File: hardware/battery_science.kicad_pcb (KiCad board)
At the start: 2 copper layers, 61 x 44.5 mm, 49 parts, among them P201 CONN_01X06, P301 CONN_01X08, P401 CONN_01X05, P402 CONN_01X05, Q301 BSS84, SW201 SPST, SW202 SPST, U201 LPC11C14, U301 BQ76925, U401 ADS1148IPWR

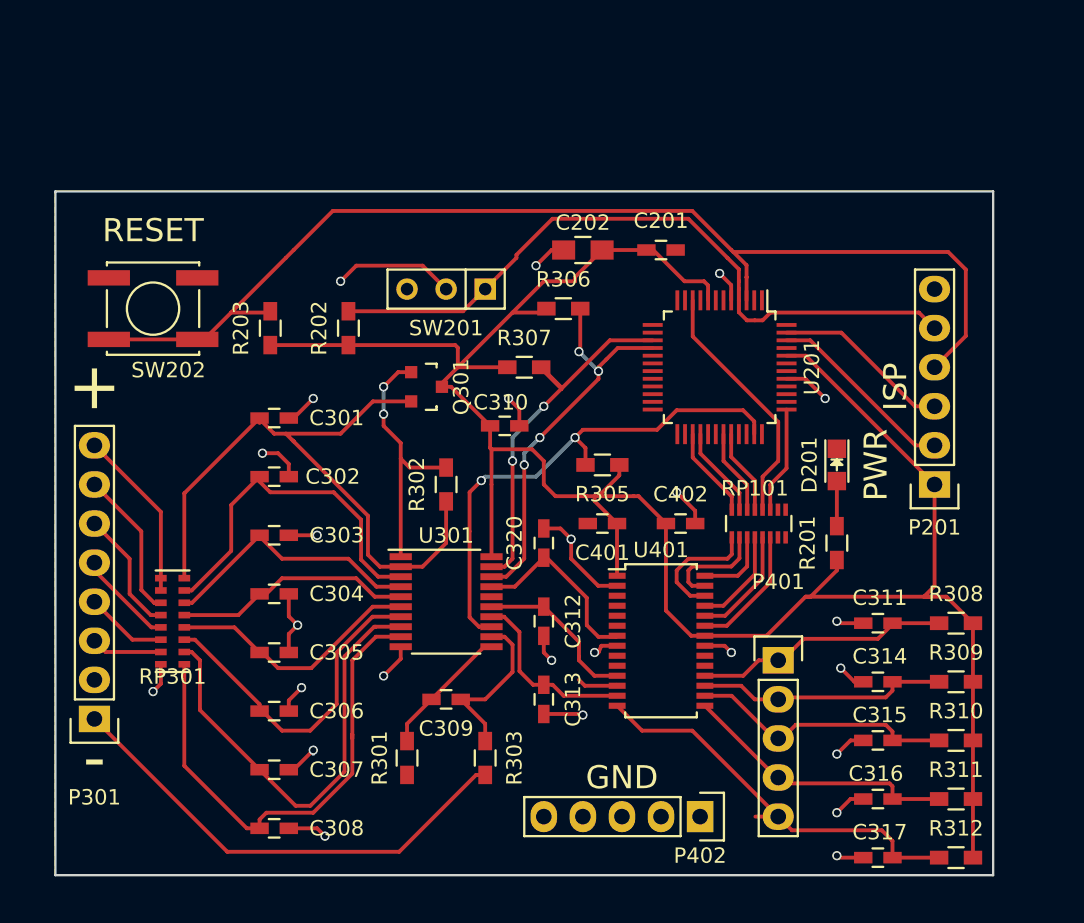
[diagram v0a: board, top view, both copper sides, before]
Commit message: Updated pcb layout
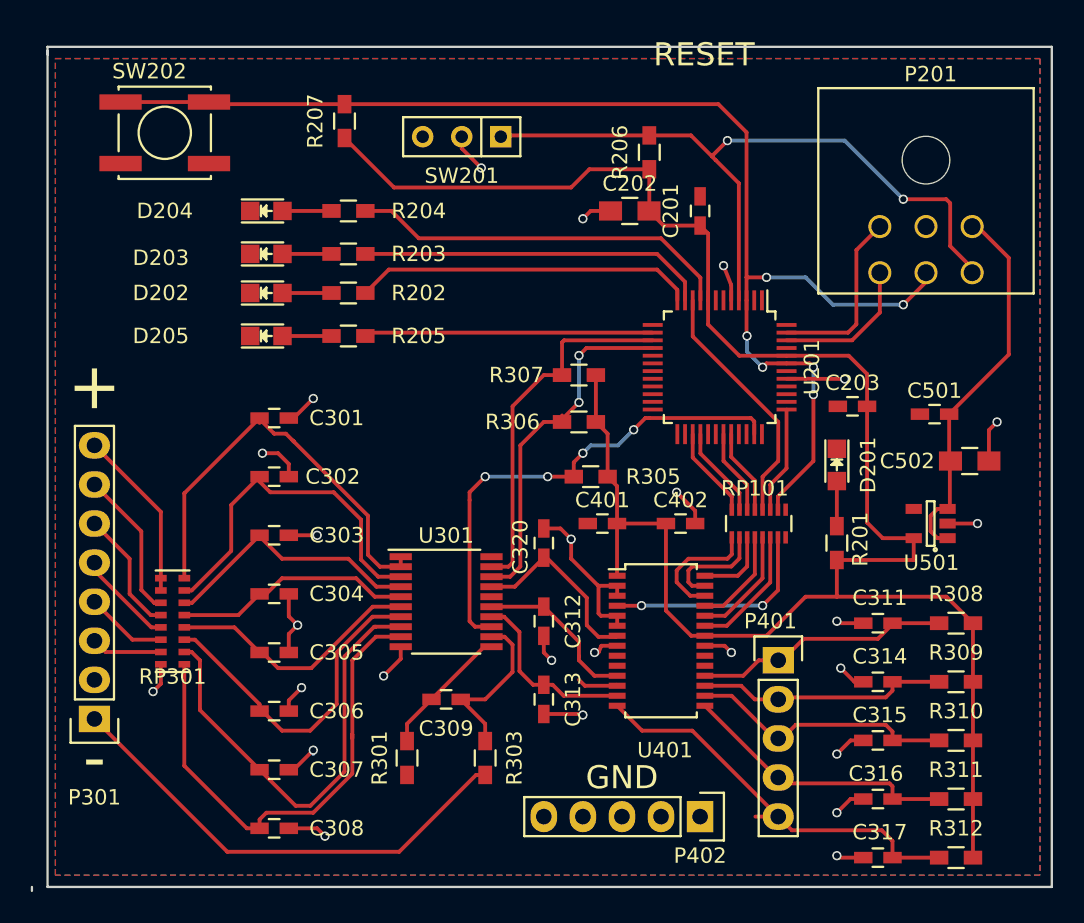
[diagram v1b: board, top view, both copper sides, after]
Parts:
- removed C310: 4.7μF, Capacitors_SMD:C_0603_HandSoldering
- removed Q301: BSS84, TO_SOT_Packages_SMD:SOT-23
- removed R302: 200k, Resistors_SMD:R_0603_HandSoldering
- added C203: .1μF, Capacitors_SMD:C_0603_HandSoldering, F.Cu at (173.7, 111.8)
- added C501: .1μF, Capacitors_SMD:C_0603_HandSoldering, F.Cu at (179.1, 112.3)
- added C502: 10μF, Capacitors_SMD:C_0805_HandSoldering, F.Cu at (181.4, 115.3)
- added D202: LED, LEDs:LED_0805, F.Cu at (135.6, 104.4)
- added D203: LED, LEDs:LED_0805, F.Cu at (135.6, 101.9)
- added D204: LED, LEDs:LED_0805, F.Cu at (135.6, 99.1)
- added D205: LED, LEDs:LED_0805, F.Cu at (135.6, 107.2)
- added R204: 100, Resistors_SMD:R_0603_HandSoldering, F.Cu at (141.0, 99.1)
- added R205: 100, Resistors_SMD:R_0603_HandSoldering, F.Cu at (141.0, 107.2)
- added R206: 10k, Resistors_SMD:R_0603_HandSoldering, F.Cu at (160.5, 95.2)
- added R207: 10k, Resistors_SMD:R_0603_HandSoldering, F.Cu at (140.7, 93.2)
- added U501: MCP1755, TO_SOT_Packages_SMD:SOT-23-5, F.Cu at (178.8, 119.4)
- P201: value CONN_01X06 -> CONN_02X03; footprint Pin_Headers:Pin_Header_Straight_1x06 -> Connectors_Molex:Molex_Microfit3_Header_02x03_Angled_43045-060x
- R202, R203: value 10k -> 100
- moved P201 17.1 mm to (175.5, 100.1)
- moved SW202 11.5 mm to (129.0, 94.0), turned to 0 degrees
- moved SW201 9.96 mm to (148.3, 94.2)
- moved R306 7.44 mm to (156.0, 112.8), turned to 180 degrees
- moved R203 7.01 mm to (141.0, 101.9), turned to 180 degrees
- moved C202 3.97 mm to (159.3, 99.1)
- moved C201 3.59 mm to (163.8, 99.1), turned to 90 degrees
- moved R307 3.59 mm to (156.0, 109.7), turned to 180 degrees
- moved R202 2.29 mm to (141.0, 104.4), turned to 180 degrees
- moved R305 1.08 mm to (156.7, 116.3)
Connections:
- P201 pad 1: +3V3 -> /microcontroller/TXD
- P201 pad 2: /microcontroller/RXD -> GND
- P201 pad 3: /microcontroller/TXD -> +5V
- P201 pad 4: /microcontroller/RESET -> /microcontroller/RXD
- P201 pad 5: /microcontroller/PROGRAM -> /microcontroller/RESET
- P201 pad 6: GND -> /microcontroller/PROGRAM
- R202 pad 1: +3V3 -> /microcontroller/LED0
- R202 pad 2: /microcontroller/PROGRAM -> Net-(D202-Pad2)
- R203 pad 1: +3V3 -> /microcontroller/LED1
- R203 pad 2: /microcontroller/RESET -> Net-(D203-Pad2)
- RP101 pad 10: Net-(RP101-Pad10) -> /microcontroller/RESET
- RP101 pad 7: Net-(RP101-Pad7) -> /ADC/Thermistors/RESET
- U201 pad 11: Net-(U201-Pad11) -> /microcontroller/LED1
- U201 pad 12: Net-(U201-Pad12) -> /microcontroller/LED0
- U201 pad 14: Net-(U201-Pad14) -> /microcontroller/LED3
- U201 pad 43: Net-(U201-Pad43) -> /microcontroller/RESET
- U201 pad 9: Net-(U201-Pad9) -> /microcontroller/LED2
- U301 pad 1: Net-(Q301-Pad1) -> Net-(C301-Pad1)
- U301 pad 20: +3V3 -> Net-(U301-Pad20)
- U401 pad 3: Net-(U401-Pad3) -> GND
- U401 pad 4: Net-(U401-Pad4) -> /ADC/Thermistors/RESET
- U401 pad 5: Net-(U401-Pad5) -> GND
- U401 pad 6: Net-(U401-Pad6) -> GND
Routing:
- net /microcontroller/LED2: track 0.00 -> 25.0 mm
- net +5V: track 0.00 -> 24.8 mm
- net /microcontroller/LED1: track 0.00 -> 22.7 mm
- net /microcontroller/LED0: track 0.00 -> 22.1 mm
- net /microcontroller/LED3: track 0.00 -> 18.8 mm
- net Net-(Q301-Pad1): track 16.9 -> 0.00 mm, vias 2 -> 0
- net +3V3: track 145.6 -> 128.8 mm
- net Net-(C301-Pad1): track 42.9 -> 28.2 mm
- net /ADC/Thermistors/RESET: track 0.00 -> 14.3 mm, vias 0 -> 2
- net /microcontroller/RESET: track 74.2 -> 84.7 mm, vias 0 -> 6
- net Net-(D205-Pad2): track 0.00 -> 3.18 mm
- net Net-(D204-Pad2): track 0.00 -> 3.18 mm
- net Net-(D203-Pad2): track 0.00 -> 3.18 mm
- net Net-(D202-Pad2): track 0.00 -> 3.18 mm
- net /microcontroller/RXD: track 12.4 -> 9.40 mm
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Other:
- board size 61 x 44.5 mm -> 66.3 x 54.9 mm
- board text removed: "ISP"
- board text removed: "PWR"
